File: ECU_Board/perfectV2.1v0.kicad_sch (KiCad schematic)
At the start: 5 parts, among them U1 Teensy4.1

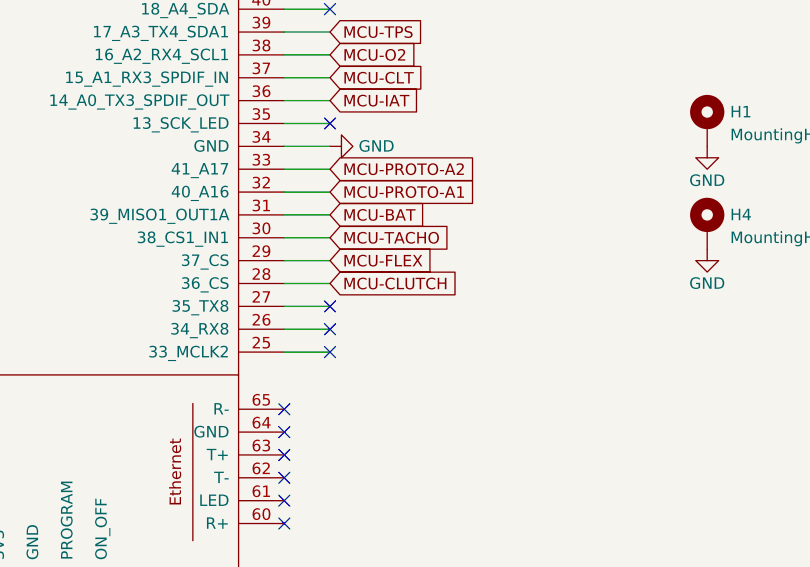
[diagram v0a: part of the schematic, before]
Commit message: Removed clutch input
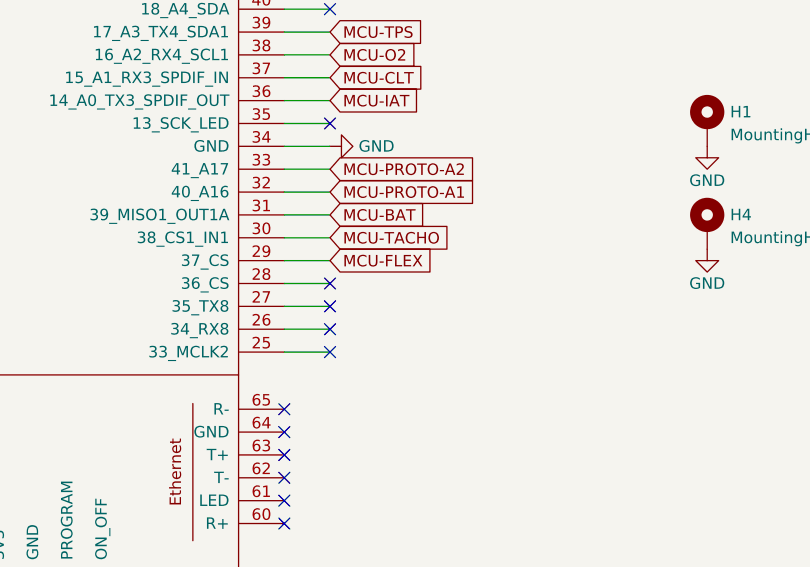
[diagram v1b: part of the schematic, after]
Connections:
- net MCU-CLUTCH: no longer names the net of U1.28 (36_CS)
- no-connect marks 25 -> 26
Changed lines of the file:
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@@
   (title_block
     (title "Speeduino board for Teensy 4.1")
-    (date "2023-01-02")
-    (rev "5")
+    (date "2023-01-07")
+    (rev "6")
     (company "Fontys Eindhoven EXPO group 13 || Speeduino")
     (comment 1 "Adapted from Speeduino V0.4.4c board")
@@
   (no_connect (at 154.94 53.34))
   (no_connect (at 149.86 29.21))
+  (no_connect (at 154.94 83.82))
   (no_connect (at 118.11 120.65))
   (no_connect (at 93.98 96.52))
@@
     (effects (font (size 1.27 1.27)) (justify left))
     (property "Intersheet References" "${INTERSHEET_REFS}" (id 0) (at 166.2431 60.8806 0)
-      (effects (font (size 1.27 1.27)) (justify left) hide)
-    )
-  )
-  (global_label "MCU-CLUTCH" (shape input) (at 154.94 83.82 0) (fields_autoplaced)
-    (effects (font (size 1.27 1.27)) (justify left))
-    (property "Intersheet References" "${INTERSHEET_REFS}" (id 0) (at 170.1741 83.7406 0)
       (effects (font (size 1.27 1.27)) (justify left) hide)
     )
@@
       (reference "#PWR0141") (unit 1) (value "GND") (footprint "")
     )
-    (path "/00000000-0000-0000-0000-00005cd18d89/00000000-0000-0000-0000-00005ce582eb"
+    (path "/bb0bb053-86b2-4a91-b561-8cb56049dc00/23c8741b-8c25-4778-8adb-5e9d1fd40157"
       (reference "#PWR0142") (unit 1) (value "GND") (footprint "")
     )
@@
       (reference "#PWR0226") (unit 1) (value "+3V3") (footprint "")
     )
-    (path "/bb0bb053-86b2-4a91-b561-8cb56049dc00/9cf9be50-832a-4dc7-90f0-ebb76430b128"
-      (reference "#PWR0227") (unit 1) (value "GND") (footprint "")
-    )
     (path "/bb0bb053-86b2-4a91-b561-8cb56049dc00/1455942a-d3ef-4554-b3fa-631a8a6d872b"
       (reference "#PWR0228") (unit 1) (value "GND") (footprint "")
@@
       (reference "D3") (unit 1) (value "PZU5.1B2A") (footprint "Diode_SMD:D_SOD-323")
     )
-    (path "/00000000-0000-0000-0000-00005cd18d89/00000000-0000-0000-0000-00005ce4be58"
-      (reference "D4") (unit 1) (value "PZU5.1B2A") (footprint "Diode_SMD:D_SOD-323")
-    )
     (path "/00000000-0000-0000-0000-00005cd18c17/00000000-0000-0000-0000-00005cd3e6c7"
       (reference "D5") (unit 1) (value "LED") (footprint "LED_SMD:LED_0805_2012Metric")
@@
       (reference "R12") (unit 1) (value "2k4R") (footprint "Resistor_SMD:R_0805_2012Metric")
     )
-    (path "/00000000-0000-0000-0000-00005cd18d89/00000000-0000-0000-0000-00005ce4ade3"
-      (reference "R13") (unit 1) (value "1kR") (footprint "Resistor_SMD:R_0402_1005Metric")
-    )
     (path "/00000000-0000-0000-0000-00006257c513/00000000-0000-0000-0000-000062600af4"

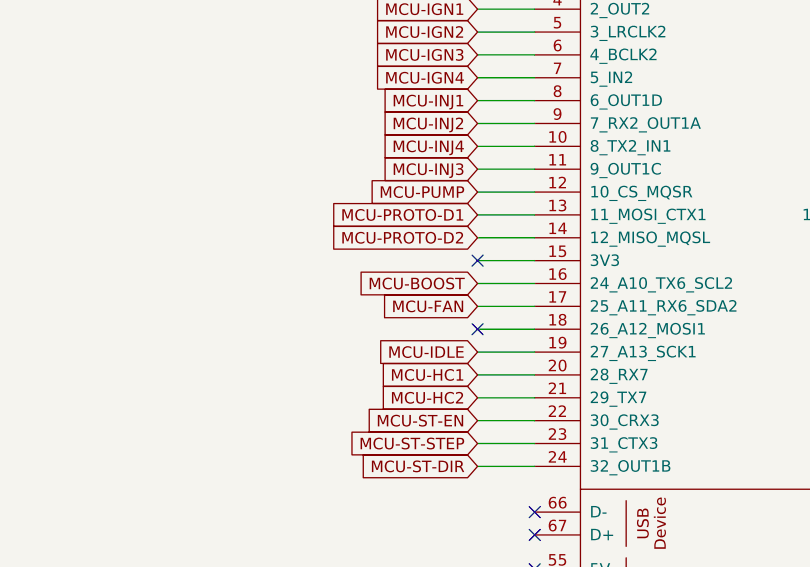
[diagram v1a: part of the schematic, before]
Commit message: Changed Boost output to ACIS
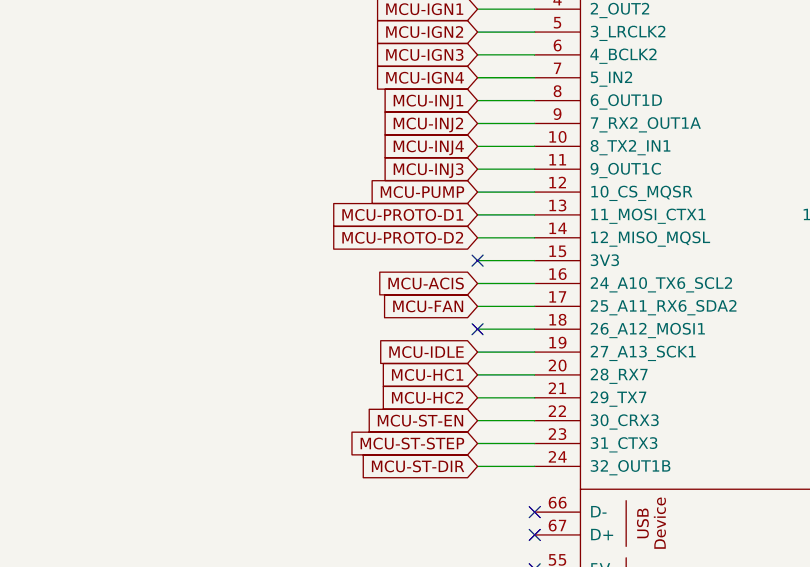
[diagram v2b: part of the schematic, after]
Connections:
- net MCU-BOOST renamed MCU-ACIS
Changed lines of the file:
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@@
     )
   )
-  (global_label "MCU-BOOST" (shape input) (at 87.63 71.12 180) (fields_autoplaced)
+  (global_label "MCU-ACIS" (shape input) (at 87.63 71.12 180) (fields_autoplaced)
     (effects (font (size 1.27 1.27)) (justify right))
-    (property "Intersheet References" "${INTERSHEET_REFS}" (id 0) (at 73.4845 71.0406 0)
+    (property "Intersheet References" "${INTERSHEET_REFS}" (id 0) (at 75.4198 71.0406 0)
       (effects (font (size 1.27 1.27)) (justify right) hide)
     )

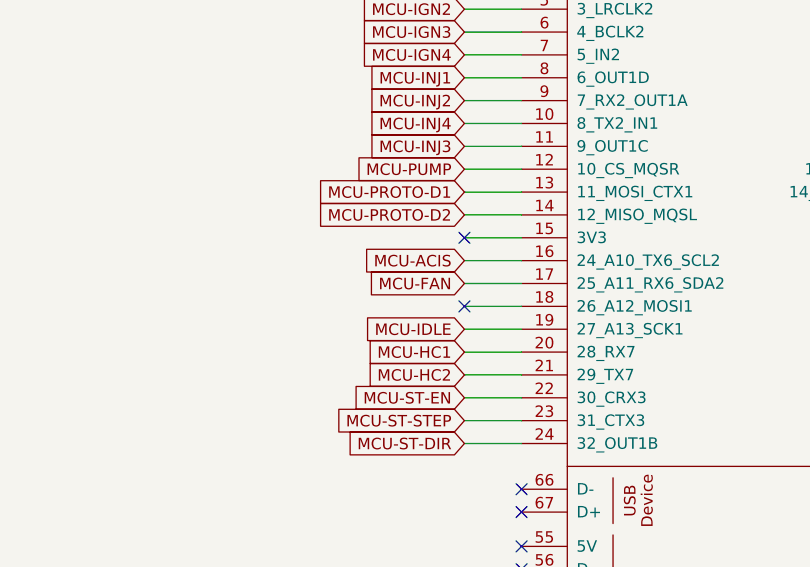
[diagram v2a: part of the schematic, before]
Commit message: Finished adapter board, slight changes to ECU
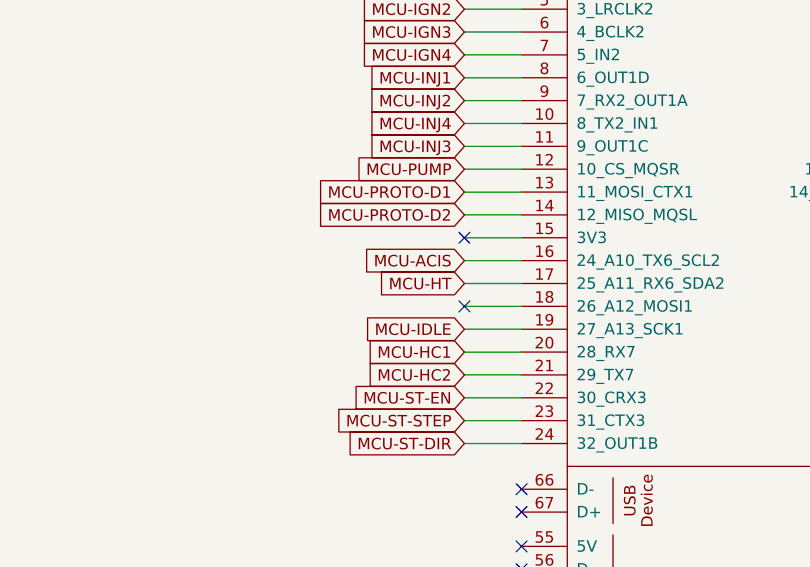
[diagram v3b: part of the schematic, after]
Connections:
- net MCU-FAN renamed MCU-HT
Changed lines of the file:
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@@
     )
   )
-  (global_label "MCU-FAN" (shape input) (at 87.63 73.66 180) (fields_autoplaced)
+  (global_label "MCU-HT" (shape input) (at 87.63 73.66 180) (fields_autoplaced)
     (effects (font (size 1.27 1.27)) (justify right))
-    (property "Intersheet References" "${INTERSHEET_REFS}" (id 0) (at 76.085 73.5806 0)
+    (property "Intersheet References" "${INTERSHEET_REFS}" (id 0) (at 77.2945 73.5806 0)
       (effects (font (size 1.27 1.27)) (justify right) hide)
     )
